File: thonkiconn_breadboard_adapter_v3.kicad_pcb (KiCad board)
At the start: 2 copper layers, 24.1 x 21 mm, 4 parts, among them J1 AudioJack2_SwitchT, J2 AudioJack2_SwitchT, J3 Conn_02x03_Odd_Even, J4 Conn_02x03_Odd_Even

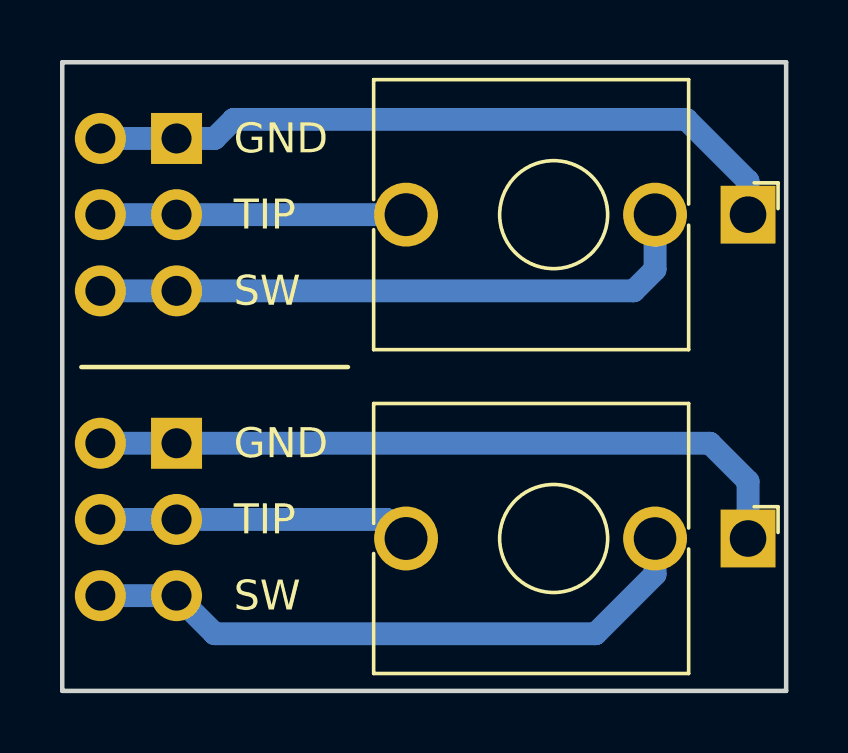
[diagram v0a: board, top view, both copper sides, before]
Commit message: Update silkscreen with github URL
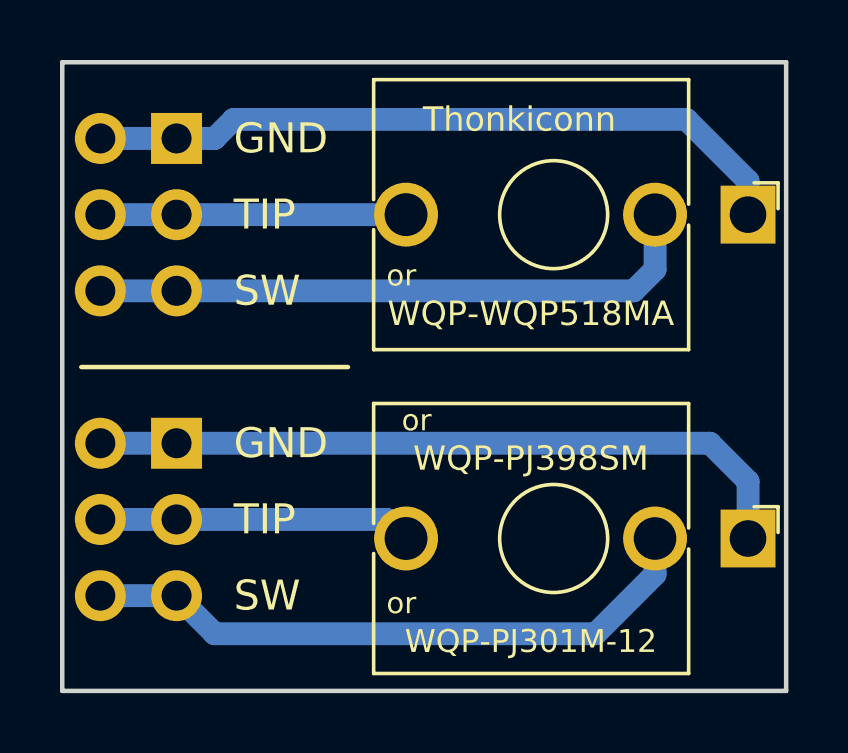
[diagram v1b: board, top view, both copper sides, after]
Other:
- board text added: "Thonkiconn"
- board text added: "Thonkiconn Breadboard Adapter V3"
- board text added: "WQP-PJ301M-12"
- board text added: "WQP-PJ398SM"
- board text added: "WQP-WQP518MA"
- board text added: "github.com/joem"
- board text added: "or"
- board text removed: "TBA V3a JWM"
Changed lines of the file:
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@@
   (general
     (thickness 1.6)
-    (drawings 12)
+    (drawings 20)
     (tracks 24)
     (zones 0)
@@
     (0 Top signal)
     (31 Bottom signal)
-    (34 B.Paste user)
-    (35 F.Paste user)
+    (34 B.Paste user hide)
+    (35 F.Paste user hide)
     (36 B.SilkS user)
     (37 F.SilkS user)
     (38 B.Mask user)
     (39 F.Mask user)
-    (40 Dwgs.User user)
-    (41 Cmts.User user)
-    (42 Eco1.User user)
-    (43 Eco2.User user)
+    (40 Dwgs.User user hide)
+    (41 Cmts.User user hide)
+    (42 Eco1.User user hide)
+    (43 Eco2.User user hide)
     (44 Edge.Cuts user)
-    (45 Margin user)
-    (46 B.CrtYd user)
-    (47 F.CrtYd user)
+    (45 Margin user hide)
+    (46 B.CrtYd user hide)
+    (47 F.CrtYd user hide)
   )
   (setup
@@
     )
   )
+  (gr_text github.com/joem (at 151.384 79.248) (layer B.SilkS)
+    (effects (font (size 0.8128 0.8128) (thickness 0.1524)) (justify mirror))
+  )
+  (gr_text or (at 149.098 84.074) (layer F.SilkS)
+    (effects (font (size 0.7112 0.7112) (thickness 0.1016)))
+  )
+  (gr_text or (at 149.606 77.978) (layer F.SilkS)
+    (effects (font (size 0.7112 0.7112) (thickness 0.1016)))
+  )
+  (gr_text or (at 149.098 73.152) (layer F.SilkS)
+    (effects (font (size 0.7112 0.7112) (thickness 0.1016)))
+  )
+  (gr_text WQP-PJ301M-12 (at 153.416 85.344) (layer F.SilkS)
+    (effects (font (size 0.762 0.762) (thickness 0.127)))
+  )
+  (gr_text WQP-PJ398SM (at 153.416 79.248) (layer F.SilkS)
+    (effects (font (size 0.8128 0.8128) (thickness 0.127)))
+  )
+  (gr_text WQP-WQP518MA (at 153.416 74.422) (layer F.SilkS)
+    (effects (font (size 0.8128 0.8128) (thickness 0.127)))
+  )
+  (gr_text Thonkiconn (at 153.035 67.945) (layer F.SilkS)
+    (effects (font (size 0.8128 0.8128) (thickness 0.1524)))
+  )
   (gr_line (start 138.43 76.2) (end 147.32 76.2) (layer F.SilkS) (width 0.15))
-  (gr_text "TBA V3a\nJWM" (at 151.13 76.2) (layer B.SilkS)
-    (effects (font (size 1 1) (thickness 0.15)) (justify mirror))
+  (gr_text "Thonkiconn Breadboard\nAdapter V3" (at 152.4 76.2) (layer B.SilkS)
+    (effects (font (size 1.016 1.016) (thickness 0.1524)) (justify mirror))
   )
   (gr_line (start 137.795 86.995) (end 161.925 86.995) (layer Edge.Cuts) (width 0.15))

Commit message: Update project to kicad 6+
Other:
- net class Default removed
